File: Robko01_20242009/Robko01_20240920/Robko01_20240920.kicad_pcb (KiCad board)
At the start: 2 copper layers, 178.8 x 143.8 mm, 62 parts, among them J1 Conn_01x04_Pin, J10 Motors, J11 Motors, J12 Conn_01x04_Pin, J13 Conn_01x02_Pin, J14 Conn_01x04_Pin, J15 Conn_01x02_Pin, J16 Conn_01x04_Pin, J17 Conn_01x02_Male, J18 Conn_01x02_Male, J19 Conn_01x01_Pin, J19 Conn_01x02_Male, J2 Conn_01x02_Pin, J20 Conn_01x01_Pin, J21 Conn_01x19_Pin, J22 Conn_01x19_Pin, J23 Conn_01x06_Pin, J24 Conn_01x04_Pin, J25 Conn_01x04_Pin, J26 Conn_01x04_Pin, J27 Conn_01x06_Pin, J28 Conn_01x02_Male, J29 Conn_01x07_Pin, J3 Conn_01x02_Pin, J30 Conn_01x02_Male, J31 Conn_01x02_Male, J4 Conn_01x04_Pin, J5 Conn_01x02_Pin, J6 Conn_01x04_Pin, J7 Conn_01x02_Male, J8 Conn_01x02_Pin, J9 Motors, K1 Relay_DPDT, SW1 SW_DIP_x05, SW2 SW_DIP_x05, SW3 SW_DIP_x05, SW4 SW_DIP_x05, SW5 SW_DIP_x05, SW6 SW_DIP_x05

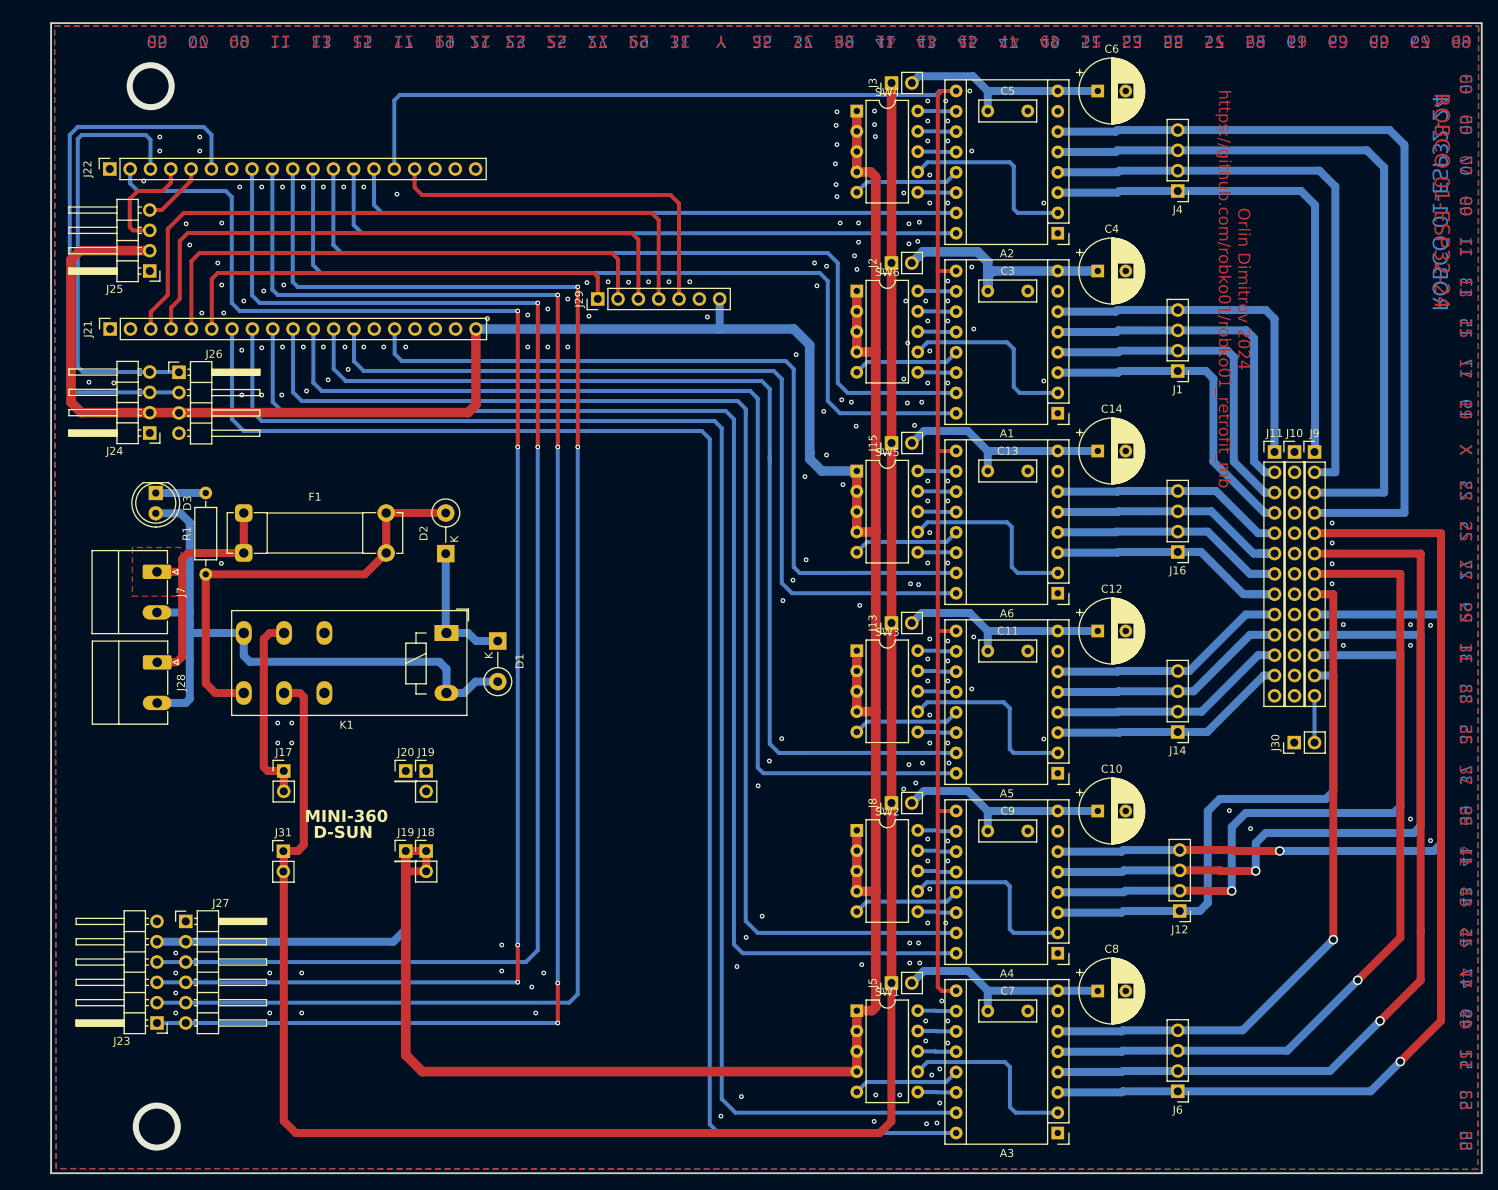
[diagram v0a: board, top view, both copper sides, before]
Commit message: Fix main MCU footprint size
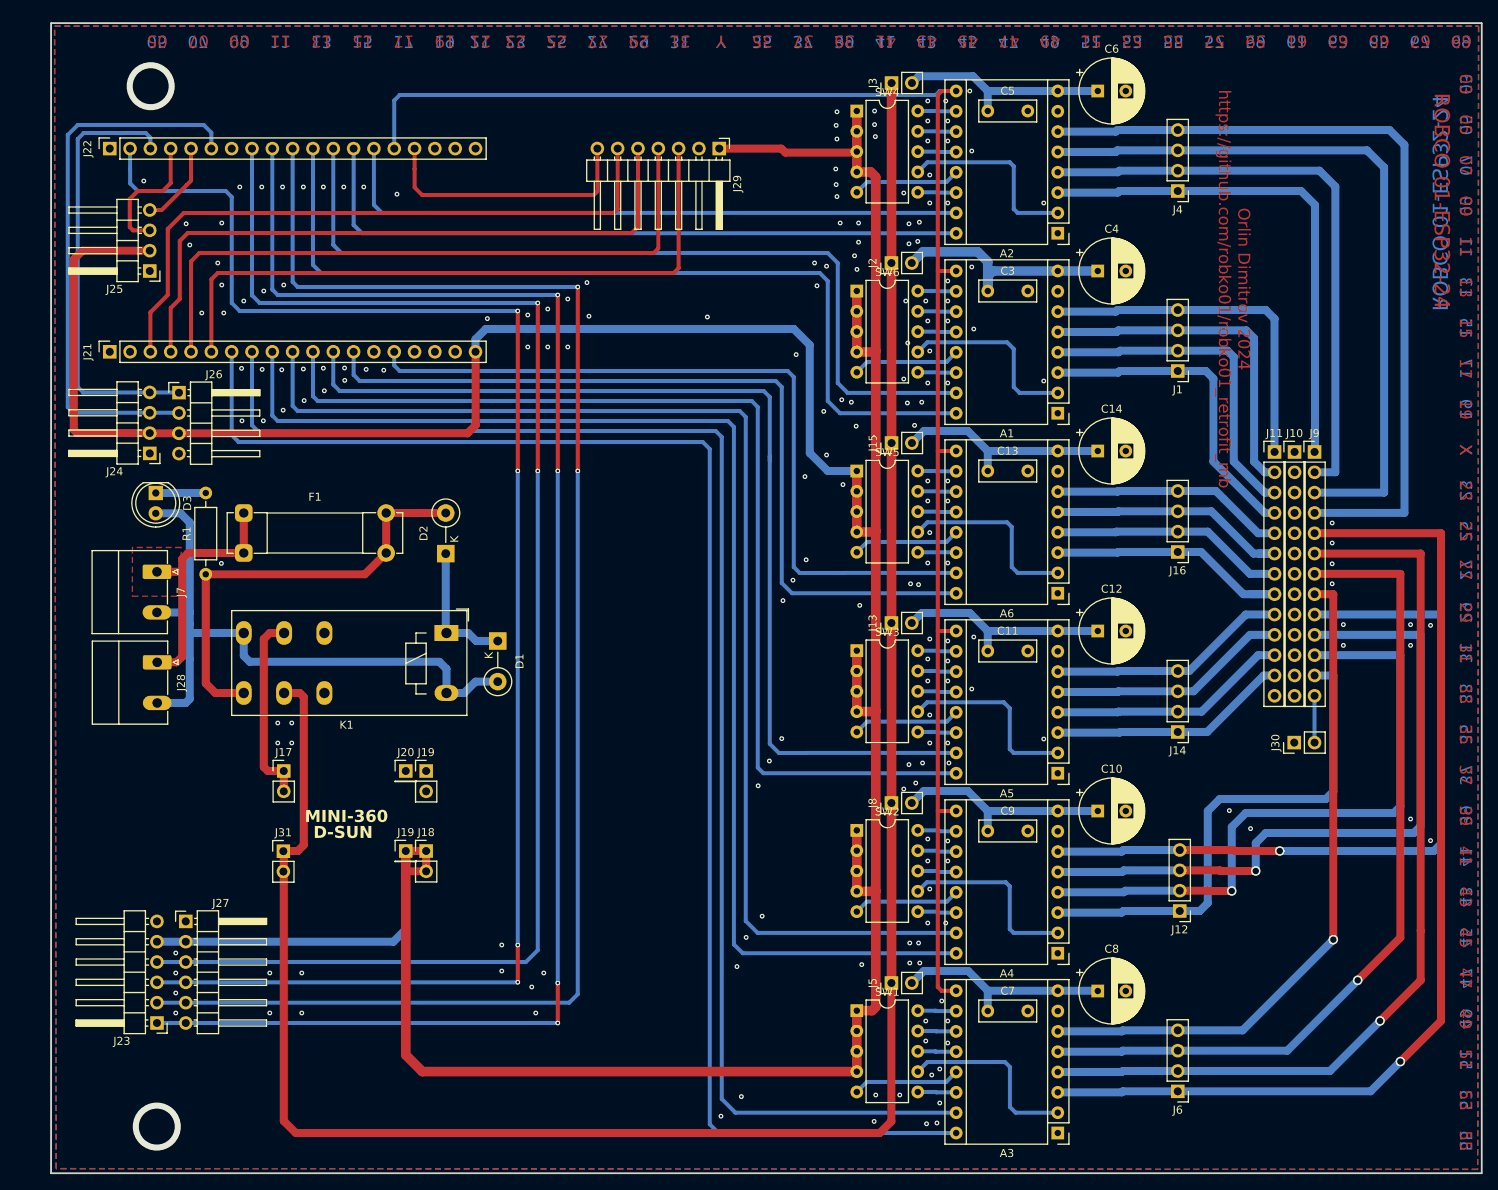
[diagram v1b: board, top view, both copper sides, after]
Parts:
- J29: footprint Connector_PinHeader_2.54mm:PinHeader_1x07_P2.54mm_Vertical -> Connector_PinHeader_2.54mm:PinHeader_1x07_P2.54mm_Horizontal
- moved J29 24.2 mm to (122.7, 32.2), turned to -90 degrees
- moved J21 2.85 mm to (46.5, 57.6)
- moved J22 2.55 mm to (46.5, 32.2)
- moved J26 2.55 mm to (55.1, 62.7)
- moved J24 2.55 mm to (51.5, 70.3)
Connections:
- J29 pad 1: GPIO35 -> +5V
- J29 pad 2: GPIO34 -> GND
- J29 pad 3: GPIO39 -> GPIO35
- J29 pad 4: GPIO36 -> GPIO34
- J29 pad 5: GPIO15 -> GPIO39
- J29 pad 6: GND -> GPIO36
- J29 pad 7: +5V -> GPIO15
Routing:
- net GPIO35: track 57.8 -> 83.0 mm
- net +5V: track 452.4 -> 470.0 mm
- net GPIO34: track 67.5 -> 82.9 mm
- net GPIO15: track 48.1 -> 33.6 mm
- net GPIO39: track 77.0 -> 82.1 mm
- net GPIO36: track 85.8 -> 81.1 mm
- net VSPI_MOSI: track 193.6 -> 196.2 mm
- net VSPI_MISO: track 181.0 -> 183.6 mm
- net STP_2: track 77.7 -> 80.2 mm
- net STP_1: track 103.8 -> 106.3 mm
- net VSPI_SS: track 191.5 -> 194.0 mm
- net VSPI_SCK: track 192.1 -> 194.7 mm
- net DIR_2: track 82.7 -> 85.3 mm
- net DIR_1: track 108.9 -> 111.4 mm
- net ENABLE: track 205.0 -> 202.5 mm
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
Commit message: Fix geometry
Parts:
- removed K1: Relay_DPDT, Relay_THT:Relay_DPDT_Schrack-RT2-FormC_RM5mm
- removed SW6: SW_DIP_x05, Package_DIP:DIP-10_W7.62mm
- added D4: LED, LED_THT:LED_D5.0mm, F.Cu at (52.2, 75.3)
- added JP1: SolderJumper_2_Bridged, Jumper:SolderJumper-2_P1.3mm_Bridged2Bar_RoundedPad1.0x1.5mm, B.Cu at (147.3, 60.9)
- added JP2: SolderJumper_2_Bridged, Jumper:SolderJumper-2_P1.3mm_Bridged2Bar_RoundedPad1.0x1.5mm, B.Cu at (147.3, 38.4)
- added JP3: SolderJumper_2_Bridged, Jumper:SolderJumper-2_P1.3mm_Bridged2Bar_RoundedPad1.0x1.5mm, B.Cu at (147.3, 150.8)
- added JP4: SolderJumper_2_Bridged, Jumper:SolderJumper-2_P1.3mm_Bridged2Bar_RoundedPad1.0x1.5mm, B.Cu at (147.3, 128.3)
- added JP5: SolderJumper_2_Bridged, Jumper:SolderJumper-2_P1.3mm_Bridged2Bar_RoundedPad1.0x1.5mm, B.Cu at (147.3, 105.8)
- added JP6: SolderJumper_2_Bridged, Jumper:SolderJumper-2_P1.3mm_Bridged2Bar_RoundedPad1.0x1.5mm, B.Cu at (147.3, 83.3)
- added K2: G5V-2, Relay_THT:Relay_DPDT_Omron_G5V-2, F.Cu at (70.5, 95.4)
- added SW7: SW_DIP_x04, Package_DIP:DIP-8_W7.62mm, F.Cu at (139.9, 50.0)
- D1, D2: footprint Diode_THT:D_DO-41_SOD81_P5.08mm_Vertical_KathodeUp -> Diode_THT:D_DO-41_SOD81_P10.16mm_Horizontal
- D3: value LED_Dual_Bidirectional -> LED; footprint LED_THT:LED_D5.0mm_Clear -> LED_THT:LED_D5.0mm
- R1: value 10k -> 2k
- SW1, SW2, SW3, SW4, SW5: value SW_DIP_x05 -> SW_DIP_x04; footprint Package_DIP:DIP-10_W7.62mm -> Package_DIP:DIP-8_W7.62mm
- moved SW1 112.4 mm to (139.9, 27.5)
- moved SW4 67.5 mm to (139.9, 95.0)
- moved SW2 22.5 mm to (139.9, 140.0)
- moved SW3 22.5 mm to (139.9, 117.4)
- moved D1 19.6 mm to (75.4, 92.9)
- moved R1 15.5 mm to (70.2, 75.2), turned to 180 degrees
- moved D2 13.4 mm to (75.4, 85.4)
- moved F1 12.2 mm to (52.4, 83.3)
- moved D3 7.03 mm to (45.7, 77.8), turned to 90 degrees
- moved J28 6.58 mm to (45.9, 96.4)
- moved J7 6.55 mm to (45.9, 85.1)
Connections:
- D3 pad 1: Net-(D3-KA) -> Net-(D1-A)
- D3 pad 2: Net-(D1-A) -> Net-(D3-A)
- R1 pad 2: Net-(D3-KA) -> Net-(D3-A)
- SW1 pad 5: Net-(A3-~{RESET}) -> Net-(A2-VDD)
- SW1 pad 6: Net-(A3-~{SLEEP}) -> Net-(A2-MS3)
- SW1 pad 7: Net-(A3-VDD) -> Net-(A2-MS2)
- SW1 pad 8: Net-(A3-MS3) -> Net-(A2-MS1)
- SW2 pad 5: Net-(A4-~{RESET}) -> Net-(A3-VDD)
- SW2 pad 6: Net-(A4-~{SLEEP}) -> Net-(A3-MS3)
- SW2 pad 7: Net-(A4-VDD) -> Net-(A3-MS2)
- SW2 pad 8: Net-(A4-MS3) -> Net-(A3-MS1)
- SW3 pad 5: Net-(A5-~{RESET}) -> Net-(A4-VDD)
- SW3 pad 6: Net-(A5-~{SLEEP}) -> Net-(A4-MS3)
- SW3 pad 7: Net-(A5-VDD) -> Net-(A4-MS2)
- SW3 pad 8: Net-(A5-MS3) -> Net-(A4-MS1)
- SW4 pad 5: Net-(A2-~{RESET}) -> Net-(A5-VDD)
- SW4 pad 6: Net-(A2-~{SLEEP}) -> Net-(A5-MS3)
- SW4 pad 7: Net-(A2-VDD) -> Net-(A5-MS2)
- SW4 pad 8: Net-(A2-MS3) -> Net-(A5-MS1)
- SW5 pad 5: Net-(A6-~{RESET}) -> Net-(A6-VDD)
- SW5 pad 6: Net-(A6-~{SLEEP}) -> Net-(A6-MS3)
- SW5 pad 7: Net-(A6-VDD) -> Net-(A6-MS2)
- SW5 pad 8: Net-(A6-MS3) -> Net-(A6-MS1)
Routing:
- net Net-(D3-A): track 0.00 -> 14.3 mm
- net Net-(D1-A): track 80.8 -> 67.5 mm
- net Net-(D2-A): track 55.1 -> 47.0 mm
- net Net-(A6-~{RESET}): track 13.5 -> 6.00 mm
- net Net-(A1-~{RESET}): track 13.5 -> 6.05 mm
- net Net-(A4-~{RESET}): track 13.4 -> 6.03 mm
- net Net-(A3-~{RESET}): track 13.5 -> 6.06 mm
- net Net-(A5-~{RESET}): track 13.4 -> 6.05 mm
- net Net-(A2-~{RESET}): track 13.5 -> 6.07 mm
- net Net-(J28-Pin_1): track 31.8 -> 25.4 mm
- net Net-(D3-KA): track 6.27 -> 0.00 mm
- net VCC: track 264.7 -> 259.9 mm
- net Net-(J17-Pin_1): track 24.1 -> 19.3 mm
- net Net-(D1-K): track 16.8 -> 13.5 mm
- net Net-(A2-~{SLEEP}): track 4.82 -> 5.56 mm
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
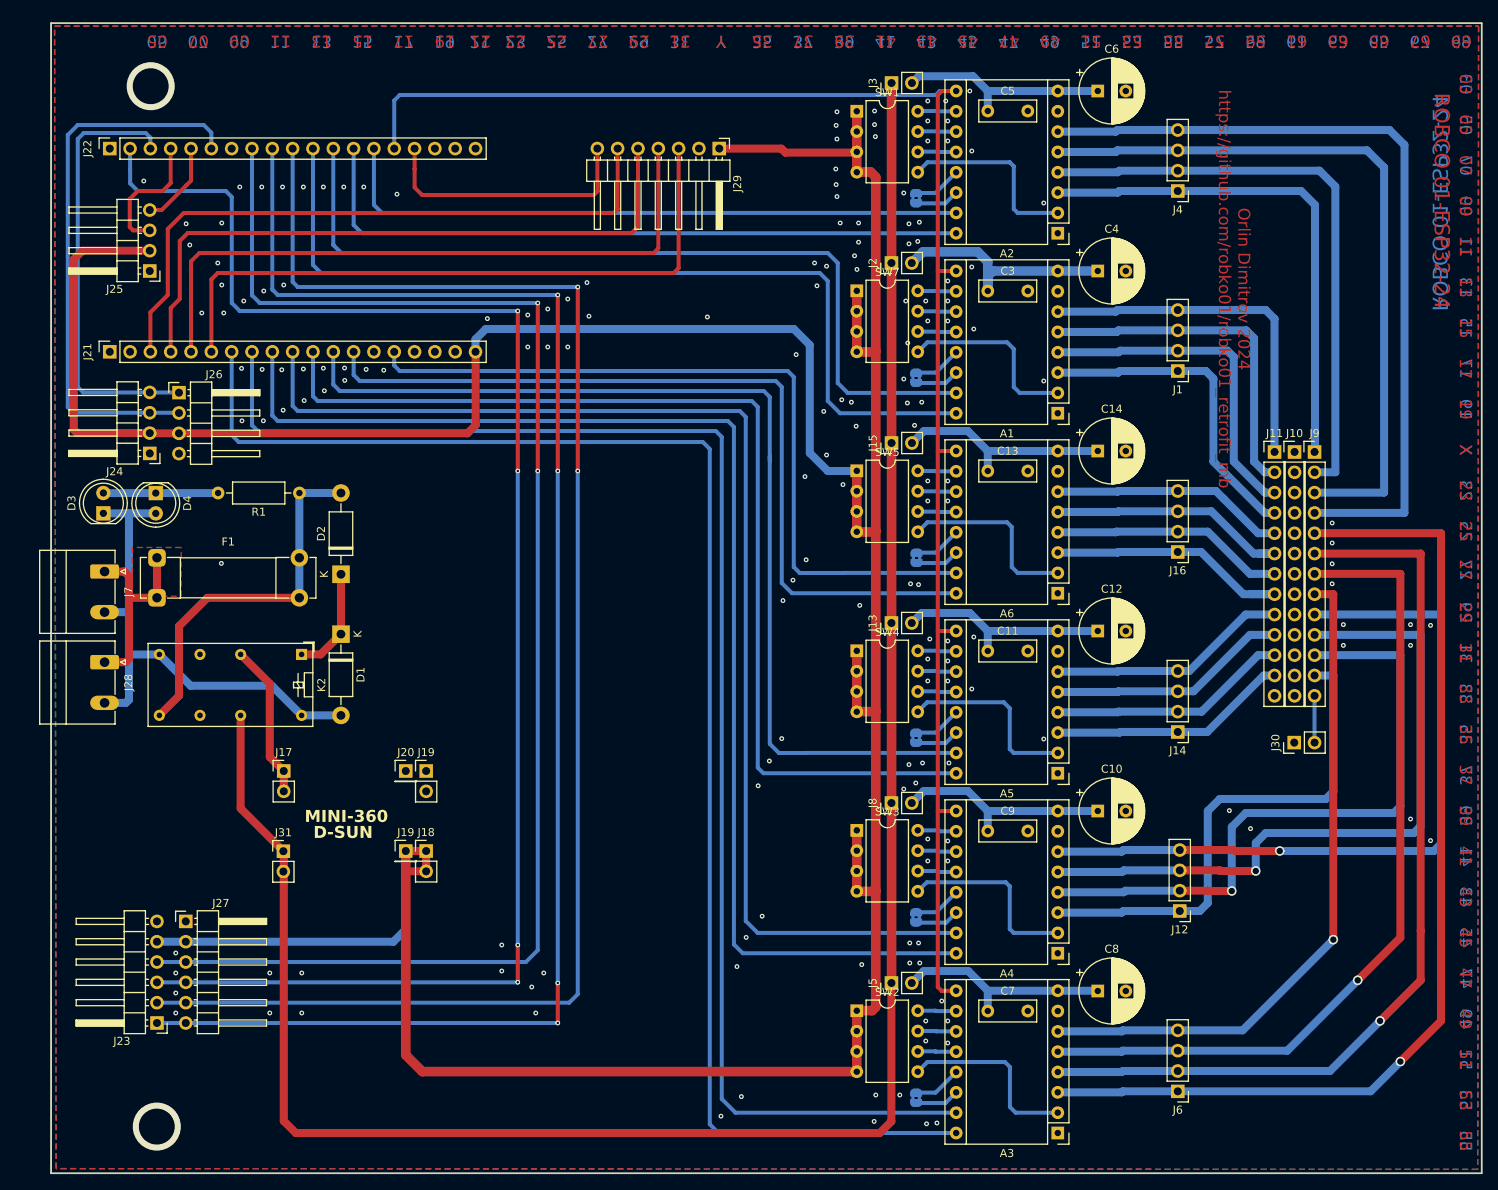
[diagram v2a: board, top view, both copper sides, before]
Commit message: Relocate elements and fix power connector positions
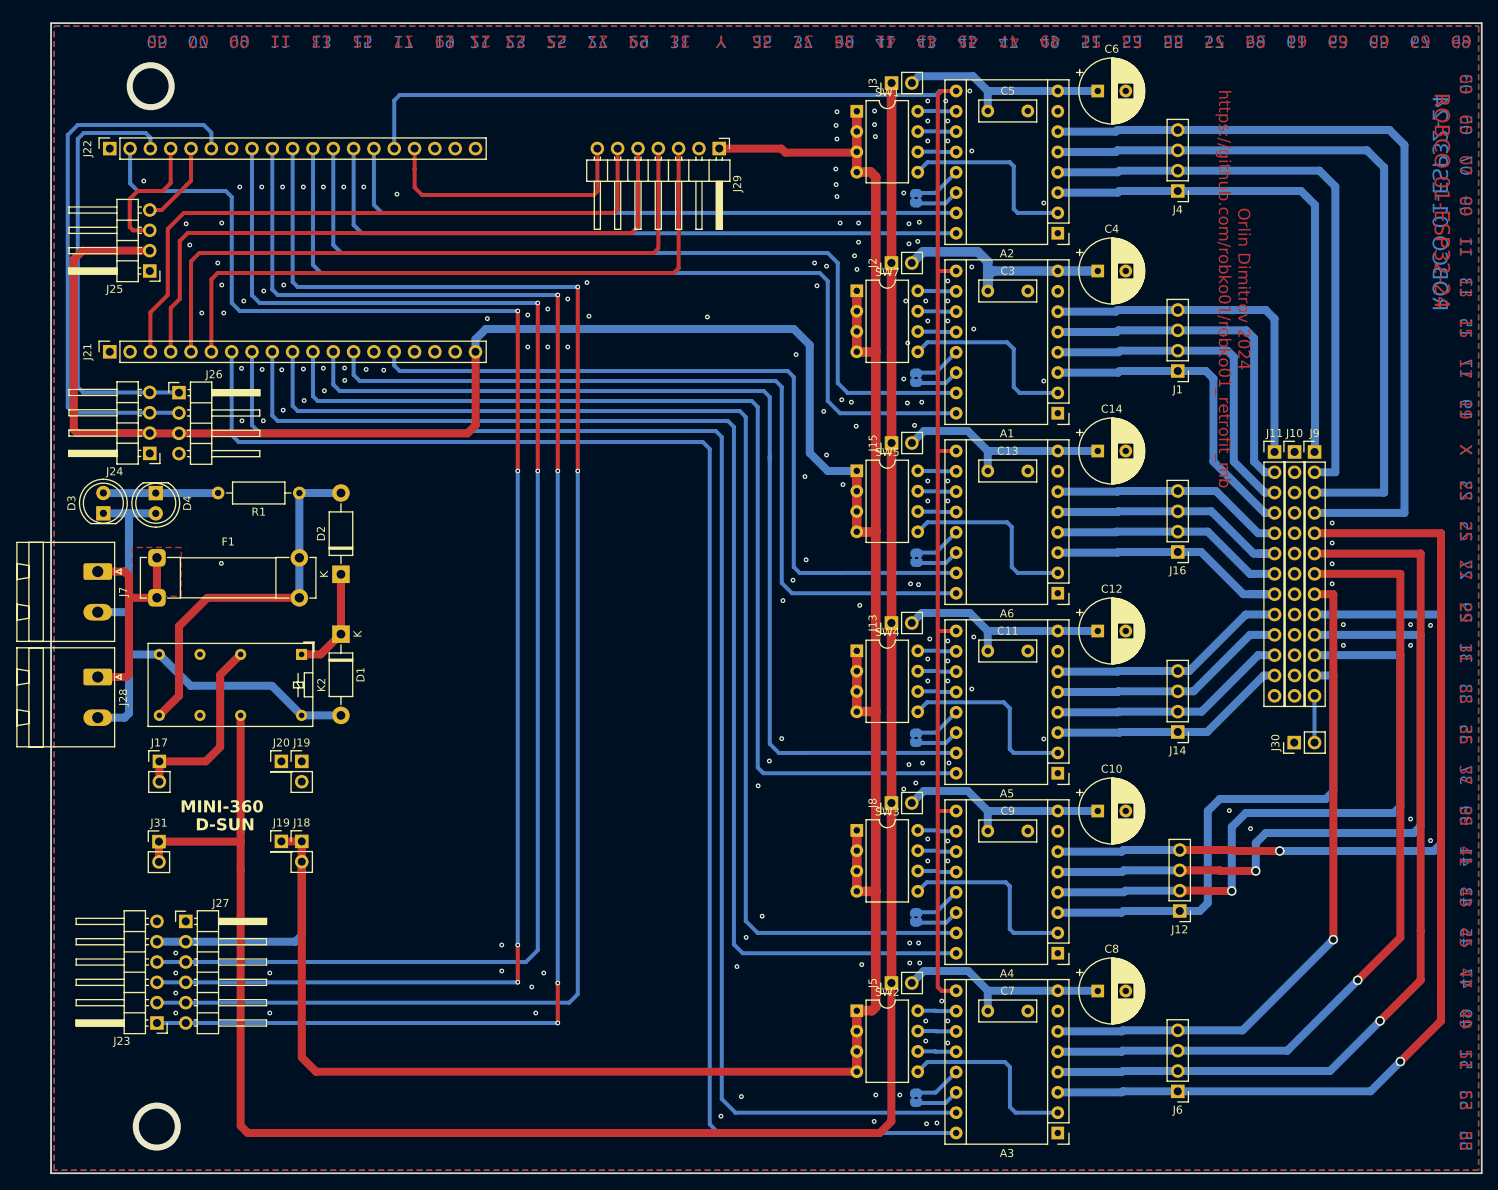
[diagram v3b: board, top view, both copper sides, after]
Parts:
- J28, J7: footprint Connector_Phoenix_MC_HighVoltage:PhoenixContact_MC_1,5_2-G-5.08_1x02_P5.08mm_Horizontal -> Connector_Phoenix_MSTB:PhoenixContact_MSTBA_2,5_2-G-5,08_1x02_P5.08mm_Horizontal
- moved J31 15.6 mm to (52.6, 118.8)
- moved J17 15.6 mm to (52.7, 108.8)
- moved J18 15.6 mm to (70.5, 118.8)
- moved J19 15.6 mm to (70.5, 108.8)
- moved J19 15.6 mm to (68.0, 118.8)
- moved J20 15.6 mm to (68.0, 108.8)
- moved J28 2.04 mm to (45.0, 98.2)
- moved J7 0.85 mm to (45.0, 85.1)
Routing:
- net VCC: track 259.9 -> 276.2 mm
- net +5V: track 470.0 -> 465.3 mm
- net Net-(J17-Pin_1): track 19.3 -> 23.5 mm
- net Net-(J28-Pin_1): track 25.4 -> 28.9 mm
- net Net-(D1-A): track 67.5 -> 71.0 mm
- net GND: vias 174 -> 172

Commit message: Add BOM
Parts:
- added J20: Conn_01x02_Male, Connector_PinHeader_2.54mm:PinHeader_1x02_P2.54mm_Vertical, F.Cu at (45.1, 113.9)

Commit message: Add small improvements
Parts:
- moved J30 2.46 mm to (192.1, 106.5)
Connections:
- net GRIPPER renamed GRIPPER_1
- J11 pad 13: GND -> GRIPPER_2
- J30 pad 1: GND -> GRIPPER_2
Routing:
- net GRIPPER_2: track 0.00 -> 5.85 mm
- net GRIPPER_1: track 5.85 -> 7.99 mm
- net GND: vias 172 -> 174
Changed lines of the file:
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@@
 	(net 1 "GND")
 	(net 2 "+5V")
-	(net 3 "GRIPPER")
+	(net 3 "GRIPPER_1")
 	(net 4 "Net-(A1-~{SLEEP})")
 	(net 5 "ENABLE")
@@
 	(net 124 "unconnected-(K2-Pad6)")
 	(net 125 "unconnected-(K2-Pad11)")
+	(net 126 "GRIPPER_2")
 	(footprint "LED_THT:LED_D5.0mm"
 		(layer "F.Cu")
@@
 	(footprint "Connector_PinHeader_2.54mm:PinHeader_1x02_P2.54mm_Vertical"
 		(layer "F.Cu")
-		(at 194.56 106.45 90)
+		(at 192.1 106.45 90)
 		(descr "Through hole straight pin header, 1x02, 2.54mm pitch, single row")
 		(tags "Through hole pin header THT 1x02 2.54mm single row")
@@
 			(layers "*.Cu" "*.Mask")
 			(remove_unused_layers no)
-			(net 1 "GND")
+			(net 126 "GRIPPER_2")
 			(pinfunction "Pin_1")
 			(pintype "passive")
@@
 			(layers "*.Cu" "*.Mask")
 			(remove_unused_layers no)
-			(net 3 "GRIPPER")
+			(net 3 "GRIPPER_1")
 			(pinfunction "Pin_2")
 			(pintype "passive")
@@
 			(layers "*.Cu" "*.Mask")
 			(remove_unused_layers no)
-			(net 1 "GND")
+			(net 126 "GRIPPER_2")
 			(pinfunction "Pin_13")
 			(pintype "passive")
@@
 			(layers "*.Cu" "*.Mask")
 			(remove_unused_layers no)
-			(net 3 "GRIPPER")
+			(net 3 "GRIPPER_1")
 			(pinfunction "Pin_13")
 			(pintype "passive")
@@
 	)
 	(via
+		(at 196 104)
+		(size 0.6)
+		(drill 0.3)
+		(layers "F.Cu" "B.Cu")
+		(free yes)
+		(net 1)
+	)
+	(via
 		(at 139.8 66.9)
 		(size 0.6)
@@
 	)
 	(via
+		(at 194 104)
+		(size 0.6)
+		(drill 0.3)
+		(layers "F.Cu" "B.Cu")
+		(free yes)
+		(net 1)
+	)
+	(via
 		(at 150.5 138.75)
 		(size 0.6)
@@
 	)
 	(segment
-		(start 197.1 106.45)
+		(start 196.55 106.45)
+		(end 197.1 105.9)
+		(width 0.5)
+		(layer "B.Cu")
+		(net 3)
+	)
+	(segment
+		(start 197.1 105.9)
 		(end 197.1 100.6)
 		(width 0.5)
@@
 	)
 	(segment
+		(start 194.64 106.45)
+		(end 196.55 106.45)
+		(width 0.5)
+		(layer "B.Cu")
+		(net 3)
+	)
+	(segment
 		(start 147.3 61.5)
 		(end 151 61.5)
@@
 		(net 123)
 	)
+	(segment
+		(start 192.1 100.6)
+		(end 192.1 106.45)
+		(width 0.5)
+		(layer "B.Cu")
+		(net 126)
+	)
 	(zone
